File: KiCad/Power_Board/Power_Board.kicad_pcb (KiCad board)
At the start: 4 copper layers, 101.6 x 63.5 mm, 170 parts, among them P1 CONN_LEFT_TOP, P10 CONN_02X01, P2 CONN_RIGHT_TOP, P3 CONN_LEFT_BOTTOM, P4 CONN_RIGHT_BOTTOM, P5 CONN_02X01, P6 CONN_02X01, P7 CONN_02X01, P8 CONN_02X01, P9 CONN_02X01, Q1 IRLL024NQ, U1 AD1583, U10 ADP7142_CSP, U11 ADP7182_CSP, U12 ADP3335_CSP, U2 MAX5259, U3 MAX5259, U4 TPS63030, U5 TPS63030, U6 TPS63030, U7 MAX152x, U8 ADP5070, U9 TPS63030

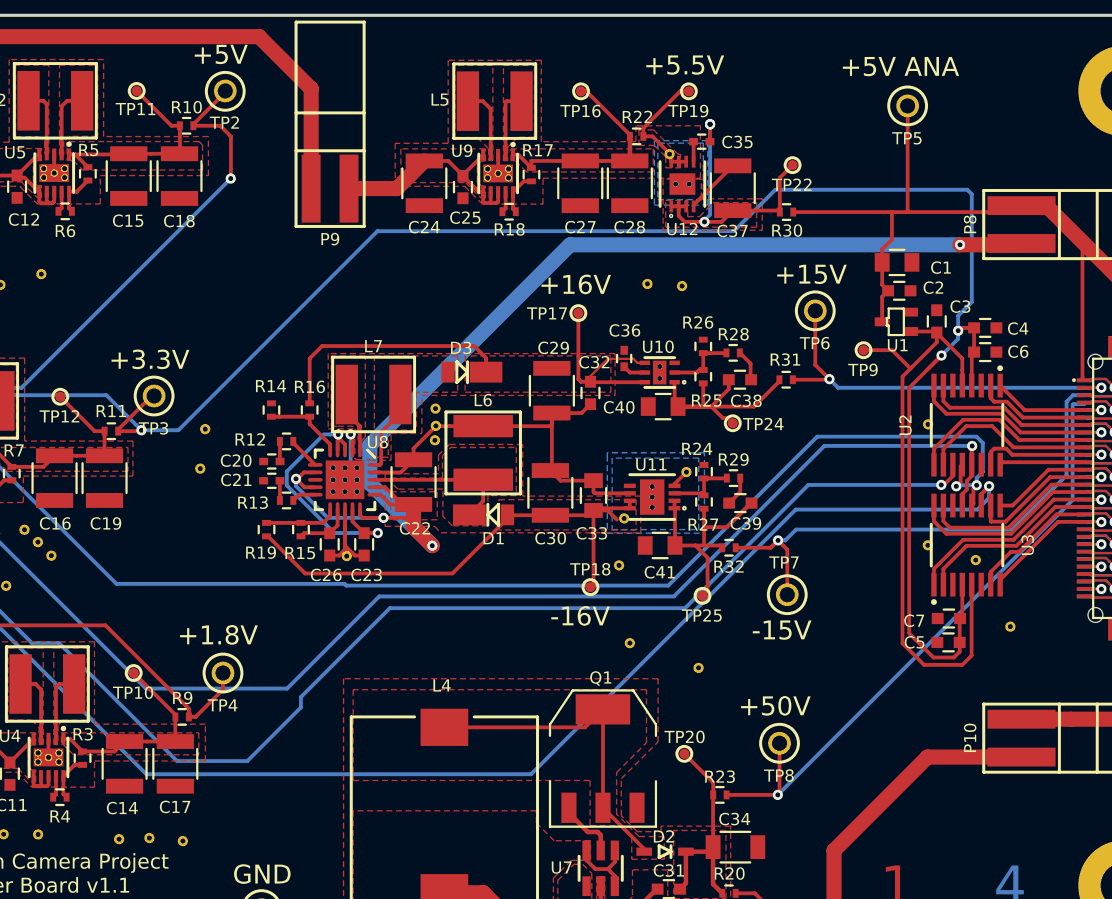
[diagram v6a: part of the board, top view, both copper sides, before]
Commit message: Component changes
Switched Vref test point to test clip.
Beefed up 0ohm jumpers to 0805.
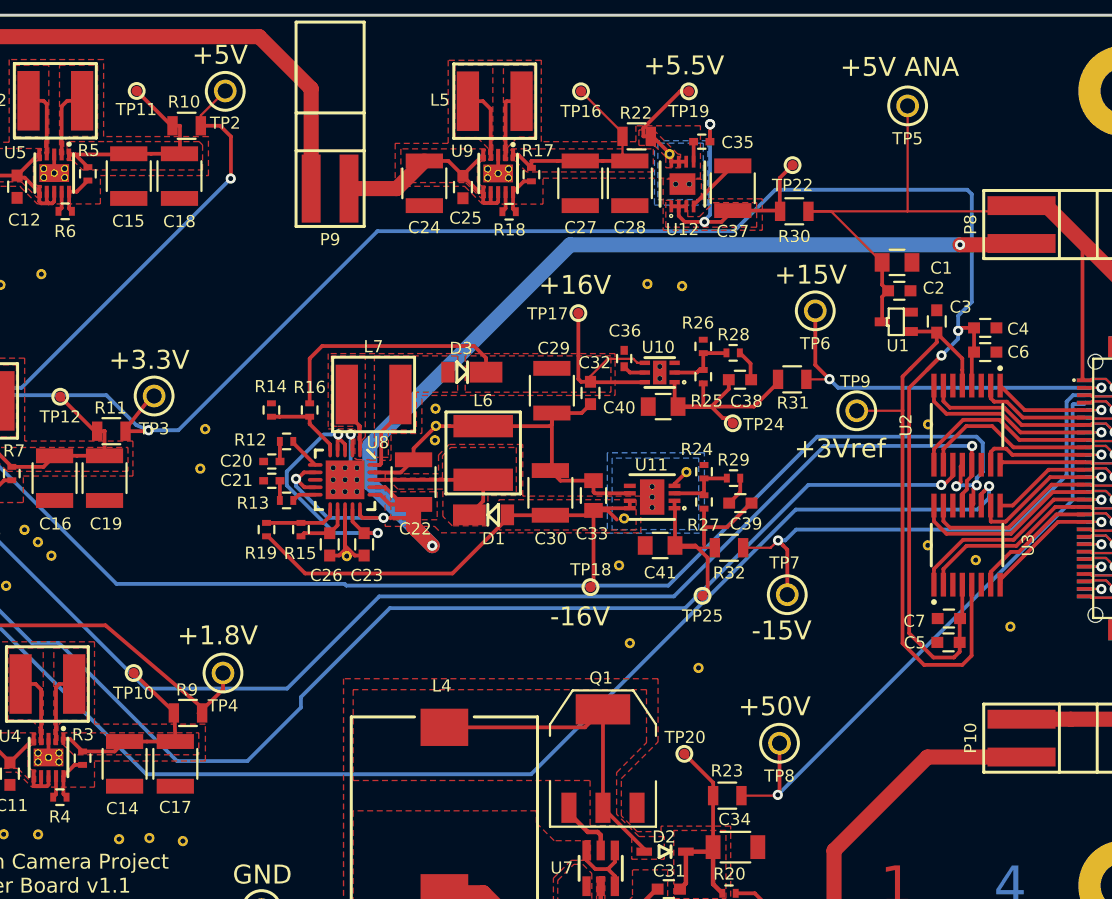
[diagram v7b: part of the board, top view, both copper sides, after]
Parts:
- R10, R11, R22, R23, R30, R31, R32, R9: footprint Resistors_SMD:R_0402 -> Resistors_SMD:R_0805
- TP9: footprint OpenCamera:TEST_POINT_SMD -> OpenCamera:TEST_CLIP
- moved TP9 4.09 mm to (167.5, 102.7)
- moved R30 0.52 mm to (163.3, 89.4)
- moved R23 0.50 mm to (158.8, 128.6)
- moved R9 0.48 mm to (122.6, 123.0)
- moved R31 0.41 mm to (163.2, 100.6)
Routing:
- net /Analog_Power/5Va: track 96.1 -> 98.4 mm
- net Net-(C39-Pad1): track 16.5 -> 17.5 mm
- net /Analog_Power/50Va: track 46.8 -> 45.8 mm
- net /Analog_Power/15Va: track 27.1 -> 26.2 mm
- net /Vref_3V: track 41.8 -> 41.2 mm
- net /Digital_Power/5V: track 45.9 -> 45.4 mm
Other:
- board text added: "+3Vref"
